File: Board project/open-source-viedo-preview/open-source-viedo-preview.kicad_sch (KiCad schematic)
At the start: 0 parts

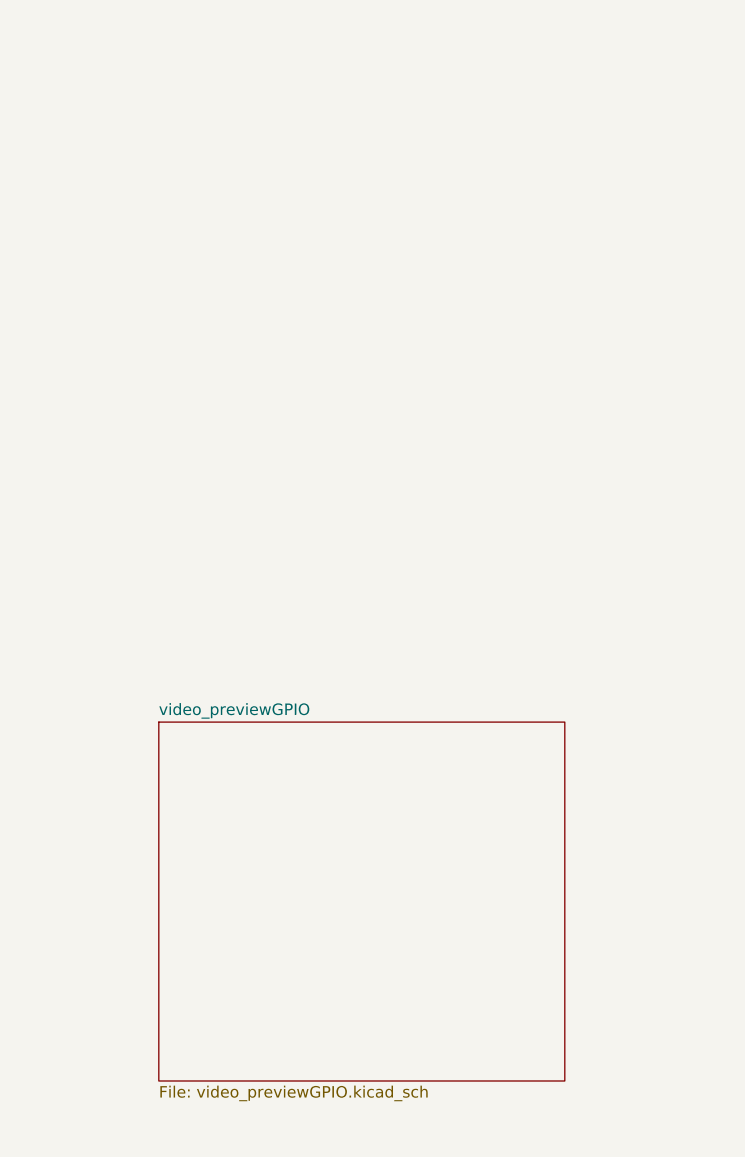
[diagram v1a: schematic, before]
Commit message: Pins 51-100 and HighSpeed part with cam connector added.
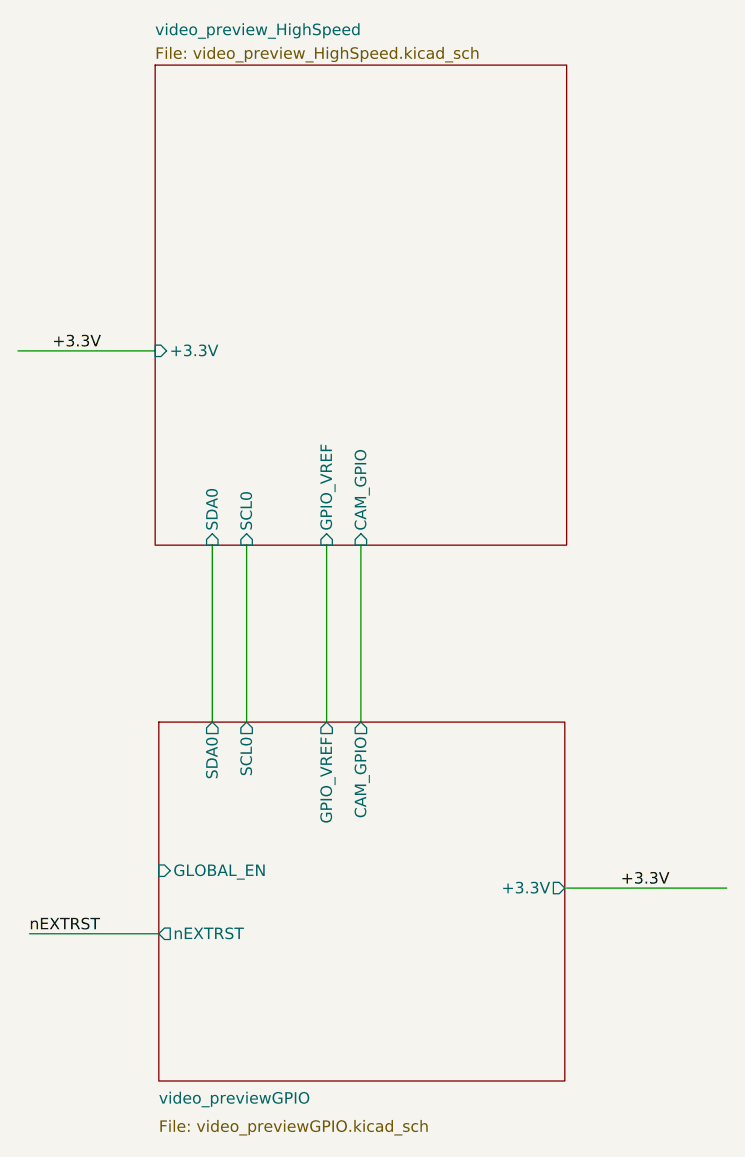
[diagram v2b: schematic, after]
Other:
- added sheet video_preview_HighSpeed (video_preview_HighSpeed.kicad_sch)
- sheet video_previewGPIO ports: added +3.3V, CAM_GPIO, GLOBAL_EN, GPIO_VREF, SCL0, SDA0, nEXTRST; removed none
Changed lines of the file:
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@@
 (kicad_sch (version 20201015) (generator eeschema)
-  (page 1 2)
   (paper "A4")
+  (wire (pts (xy 87.63 67.31) (xy 102.87 67.31))
+    (stroke (width 0) (type solid) (color 0 0 0 0))
+  )
+  (wire (pts (xy 88.9 132.08) (xy 103.2764 132.08))
+    (stroke (width 0) (type solid) (color 0 0 0 0))
+  )
+  (wire (pts (xy 109.22 88.9) (xy 109.22 108.5596))
+    (stroke (width 0) (type solid) (color 0 0 0 0))
+  )
+  (wire (pts (xy 113.03 88.9) (xy 113.03 108.5596))
+    (stroke (width 0) (type solid) (color 0 0 0 0))
+  )
+  (wire (pts (xy 121.92 88.9) (xy 121.92 108.5596))
+    (stroke (width 0) (type solid) (color 0 0 0 0))
+  )
+  (wire (pts (xy 125.73 88.9) (xy 125.73 108.5596))
+    (stroke (width 0) (type solid) (color 0 0 0 0))
+  )
+  (wire (pts (xy 148.59 127) (xy 166.37 127))
+    (stroke (width 0) (type solid) (color 0 0 0 0))
+  )
+  (label "nEXTRST" (at 88.9 132.08 0)
+    (effects (font (size 1.27 1.27)) (justify left bottom))
+  )
+  (label "+3.3V" (at 91.44 67.31 0)
+    (effects (font (size 1.27 1.27)) (justify left bottom))
+  )
+  (label "+3.3V" (at 160.02 127 180)
+    (effects (font (size 1.27 1.27)) (justify right bottom))
+  )
   (sheet (at 103.2764 108.5596) (size 45.1104 39.878)
     (stroke (width 0.001) (type solid) (color 132 0 132 1))
     (fill (color 255 255 255 0.0000))
-    (property "Nazwa arkusza" "video_previewGPIO" (id 0) (at 103.2764 107.9237 0)
+    (property "Nazwa arkusza" "video_previewGPIO" (id 0) (at 103.2764 151.1037 0)
       (effects (font (size 1.27 1.27)) (justify left bottom))
     )
-    (property "Sheet file" "video_previewGPIO.kicad_sch" (id 1) (at 103.2764 148.9465 0)
+    (property "Sheet file" "video_previewGPIO.kicad_sch" (id 1) (at 103.2764 152.7565 0)
       (effects (font (size 1.27 1.27)) (justify left top))
+    )
+    (pin "GPIO_VREF" output (at 121.92 108.5596 90)
+      (effects (font (size 1.27 1.27)) (justify right))
+    )
+    (pin "GLOBAL_EN" input (at 103.2764 125.0696 180)
+      (effects (font (size 1.27 1.27)) (justify left))
+    )
+    (pin "CAM_GPIO" output (at 125.73 108.5596 90)
+      (effects (font (size 1.27 1.27)) (justify right))
+    )
+    (pin "nEXTRST" output (at 103.2764 132.08 180)
+      (effects (font (size 1.27 1.27)) (justify left))
+    )
+    (pin "SDA0" output (at 109.22 108.5596 90)
+      (effects (font (size 1.27 1.27)) (justify right))
+    )
+    (pin "SCL0" output (at 113.03 108.5596 90)
+      (effects (font (size 1.27 1.27)) (justify right))
+    )
+    (pin "+3.3V" output (at 148.3868 127 0)
+      (effects (font (size 1.27 1.27)) (justify right))
+    )
+  )
+  (sheet (at 102.87 35.56) (size 45.72 53.34)
+    (stroke (width 0.001) (type solid) (color 132 0 132 1))
+    (fill (color 255 255 255 0.0000))
+    (property "Nazwa arkusza" "video_preview_HighSpeed" (id 0) (at 102.87 32.3841 0)
+      (effects (font (size 1.27 1.27)) (justify left bottom))
+    )
+    (property "Sheet file" "video_preview_HighSpeed.kicad_sch" (id 1) (at 102.87 33.5289 0)
+      (effects (font (size 1.27 1.27)) (justify left top))
+    )
+    (pin "CAM_GPIO" input (at 125.73 88.9 270)
+      (effects (font (size 1.27 1.27)) (justify left))
+    )
+    (pin "SCL0" input (at 113.03 88.9 270)
+      (effects (font (size 1.27 1.27)) (justify left))
+    )
+    (pin "SDA0" input (at 109.22 88.9 270)
+      (effects (font (size 1.27 1.27)) (justify left))
+    )
+    (pin "GPIO_VREF" input (at 121.92 88.9 270)
+      (effects (font (size 1.27 1.27)) (justify left))
+    )
+    (pin "+3.3V" input (at 102.87 67.31 180)
+      (effects (font (size 1.27 1.27)) (justify left))
     )
   )
@@
     (path "/" (page "1"))
     (path "/b730802d-9d6d-43fe-b6ab-71910814cd57/" (page "2"))
+    (path "/fbc78747-3566-4228-ab41-be6ba2cba6e4/" (page "3"))
   )
   (symbol_instances
@@
       (reference "#PWR04") (unit 1) (value "GND") (footprint "")
     )
-    (path "/b730802d-9d6d-43fe-b6ab-71910814cd57/cb7bd3ce-482e-4699-bc8c-34397f93e291"
-      (reference "#PWR05") (unit 1) (value "+3V3") (footprint "")
-    )
     (path "/b730802d-9d6d-43fe-b6ab-71910814cd57/03d92291-834c-46f6-959c-62e2dd3be9ab"
       (reference "#PWR06") (unit 1) (value "GND") (footprint "")
@@
     (path "/b730802d-9d6d-43fe-b6ab-71910814cd57/96ff48db-662d-4c24-a5ae-a0fb3fe7e0f9"
       (reference "#PWR07") (unit 1) (value "GND") (footprint "")
-    )
-    (path "/b730802d-9d6d-43fe-b6ab-71910814cd57/98b1999e-0c2c-4ffb-bd15-84e62b020b2a"
-      (reference "#PWR08") (unit 1) (value "+3V3") (footprint "")
     )
     (path "/b730802d-9d6d-43fe-b6ab-71910814cd57/cce6548a-6b8b-4e7d-ab93-4a56475727ad"
@@
       (reference "#PWR011") (unit 1) (value "+5V") (footprint "")
     )
+    (path "/b730802d-9d6d-43fe-b6ab-71910814cd57/979bd904-748a-44c8-8d0c-2af4e5b58a0d"
+      (reference "#PWR012") (unit 1) (value "GND") (footprint "")
+    )
+    (path "/b730802d-9d6d-43fe-b6ab-71910814cd57/ae66d566-01b3-4561-a155-79c997fa6efb"
+      (reference "#PWR013") (unit 1) (value "GND") (footprint "")
+    )
+    (path "/b730802d-9d6d-43fe-b6ab-71910814cd57/1be4e34f-29ea-4e72-a6a9-63562c7f203a"
+      (reference "#PWR014") (unit 1) (value "GND") (footprint "")
+    )
     (path "/b730802d-9d6d-43fe-b6ab-71910814cd57/ad6a9713-2347-49d2-931e-f61931162123"
       (reference "#PWR0101") (unit 1) (value "GND") (footprint "")
-    )
-    (path "/b730802d-9d6d-43fe-b6ab-71910814cd57/8d85e7d4-2f18-4f0f-ba8b-0f24d387fd15"
-      (reference "#PWR0102") (unit 1) (value "+3V3") (footprint "")
     )
     (path "/b730802d-9d6d-43fe-b6ab-71910814cd57/4de35d08-ff35-40bc-8bf2-6129439c541b"
@@
     (path "/b730802d-9d6d-43fe-b6ab-71910814cd57/e1db2a41-85ad-457d-9dac-46a10eae26dd"
       (reference "D1") (unit 1) (value "Green LED") (footprint "")
+    )
+    (path "/b730802d-9d6d-43fe-b6ab-71910814cd57/d88a3934-0c45-46ed-9ff8-c9ce835c0285"
+      (reference "D2") (unit 1) (value "LED Red") (footprint "LED_SMD:LED_0603_1608Metric")
     )
     (path "/b730802d-9d6d-43fe-b6ab-71910814cd57/52f646bc-4dc9-4f08-8d4b-f132d285ff7b"
@@
     (path "/b730802d-9d6d-43fe-b6ab-71910814cd57/f6c1126e-54b8-46f7-8022-f16e670117f9"
       (reference "J3") (unit 1) (value "Conn_02x20_Odd_Even") (footprint "")
+    )
+    (path "/b730802d-9d6d-43fe-b6ab-71910814cd57/87fd25a4-f4fa-4003-91b7-2873f9d0e853"
+      (reference "J4") (unit 1) (value "Conn_01x03") (footprint "Connector_PinHeader_2.54mm:PinHeader_1x03_P2.54mm_Vertical")
+    )
+    (path "/b730802d-9d6d-43fe-b6ab-71910814cd57/0381caf2-0b92-4e63-97ce-b0bc94e34a8f"
+      (reference "J5") (unit 1) (value "Conn_01x03") (footprint "Connector_PinHeader_2.54mm:PinHeader_1x03_P2.54mm_Vertical")
     )
     (path "/b730802d-9d6d-43fe-b6ab-71910814cd57/50af4ba0-8c70-439c-afb7-b864ba5ef62f"
@@
       (reference "R3") (unit 1) (value "1k") (footprint "")
     )
+    (path "/b730802d-9d6d-43fe-b6ab-71910814cd57/90efc3c5-de08-465e-b474-f1a62f5d9538"
+      (reference "R4") (unit 1) (value "1k") (footprint "Resistor_SMD:R_0402_1005Metric")
+    )
+    (path "/b730802d-9d6d-43fe-b6ab-71910814cd57/95c07a55-2795-4a61-b671-b32b4b65b768"
+      (reference "R5") (unit 1) (value "0R") (footprint "Resistor_SMD:R_0805_2012Metric_Pad1.15x1.40mm_HandSolder")
+    )
+    (path "/b730802d-9d6d-43fe-b6ab-71910814cd57/ddc359fd-0e58-4a1b-a4be-b64e010bc66b"
+      (reference "R6") (unit 1) (value "nf") (footprint "Resistor_SMD:R_0805_2012Metric_Pad1.15x1.40mm_HandSolder")
+    )
+    (path "/b730802d-9d6d-43fe-b6ab-71910814cd57/e6fc67f5-88fb-469d-bdc0-b62ffdc2c09a"
+      (reference "U1") (unit 1) (value "74LVC1G07") (footprint "Package_TO_SOT_SMD:SOT-353_SC-70-5_Handsoldering")
+    )
+    (path "/b730802d-9d6d-43fe-b6ab-71910814cd57/0f96da05-3d95-4795-96bc-ee3a95c8b6b9"
+      (reference "U2") (unit 1) (value "74LVC1G07") (footprint "Package_TO_SOT_SMD:SOT-353_SC-70-5_Handsoldering")
+    )
+    (path "/fbc78747-3566-4228-ab41-be6ba2cba6e4/853b0d29-49e4-407d-9374-5eb6a88773b1"
+      (reference "#PWR015") (unit 1) (value "GND") (footprint "")
+    )
+    (path "/fbc78747-3566-4228-ab41-be6ba2cba6e4/3e4a45d5-a332-4c81-96cf-e203419f8297"
+      (reference "J6") (unit 1) (value "Conn_01x22_Female") (footprint "Connector_FFC-FPC:Hirose_FH12-22S-0.5SH_1x22-1MP_P0.50mm_Horizontal")
+    )
   )

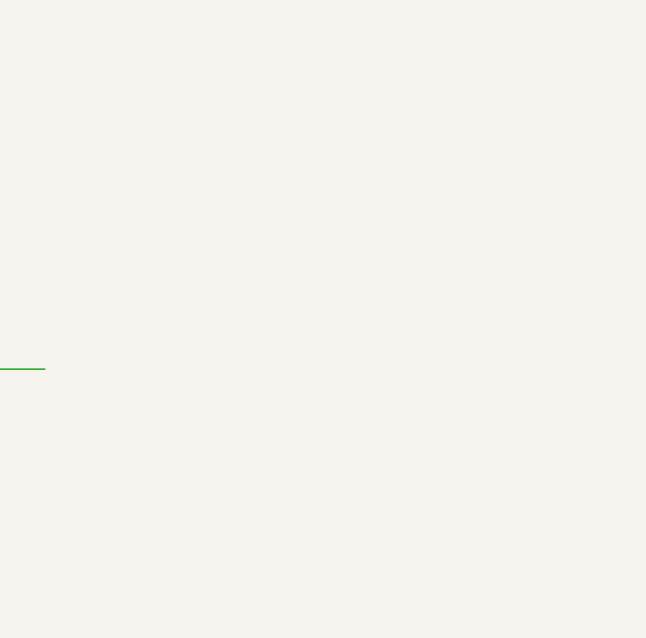
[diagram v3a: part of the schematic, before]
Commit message: PSU added
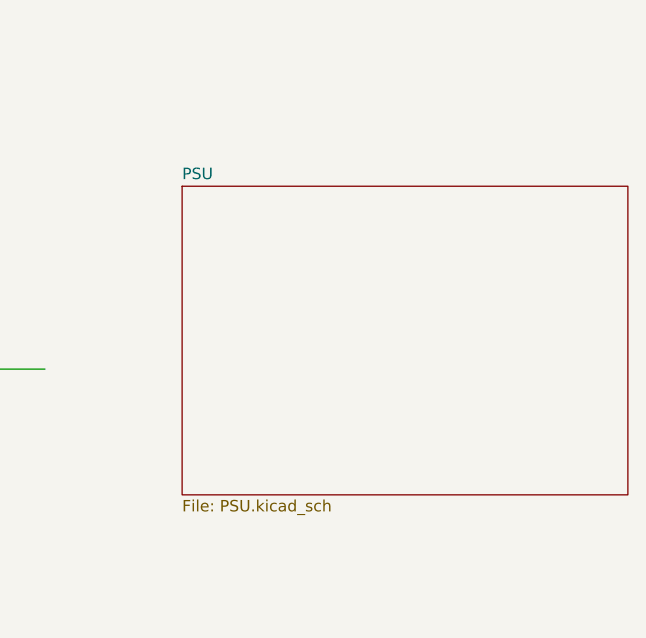
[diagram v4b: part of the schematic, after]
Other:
- added sheet PSU (PSU.kicad_sch)

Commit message: pin 101-150
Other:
- added sheet pcie (untitled.kicad_sch)
- added sheet usb-otg (usb-otg.kicad_sch)

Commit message: Imporoved electrical schematic
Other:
- sheet pcie ports: added PCIE_CLK_N, PCIE_CLK_P, PCIE_CLK_nREQ, PCIE_RX_N, PCIE_RX_P, PCIE_TX_N, PCIE_TX_P, PCIE_nRST; removed none
- sheet usb-otg ports: added USB2_N, USB2_P, USBOTG; removed none
- sheet video_previewGPIO ports: added none; removed +3.3V
- sheet video_preview_HighSpeed ports: added PCIE_CLK_N, PCIE_CLK_P, PCIE_CLK_nREQ, PCIE_RX_N, PCIE_RX_P, PCIE_TX_N, PCIE_TX_P, PCIE_nRST, USB2_N, USB2_P, USBOTG_ID; removed +3.3V
